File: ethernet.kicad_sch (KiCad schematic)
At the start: 1 part

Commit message: write some things down
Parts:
- U1: renamed from U?; value MCIMX6YxxVMxxxx -> MCIMX6Y2DVM09AB; Manufacturer (none) -> NXP; MfgPartNo (none) -> MCIMX6Y2DVM09AB; Vendor (none) -> Digi-Key; VendorPartNo (none) -> 568-14995-ND
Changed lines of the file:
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@@
   (symbol (lib_id "catfood:MCIMX6YxxVMxxxx") (at 55.88 53.34 0) (unit 8)
     (in_bom yes) (on_board yes) (fields_autoplaced)
-    (property "Reference" "U?" (id 0) (at 55.88 21.59 0))
-    (property "Value" "MCIMX6YxxVMxxxx" (id 1) (at 55.88 24.13 0))
+    (property "Reference" "U1" (id 0) (at 55.88 21.59 0))
+    (property "Value" "MCIMX6Y2DVM09AB" (id 1) (at 55.88 24.13 0))
     (property "Footprint" "" (id 2) (at 45.72 34.29 0)
       (effects (font (size 1.27 1.27)) hide)
@@
       (effects (font (size 1.27 1.27)) hide)
     )
+    (property "Manufacturer" "NXP" (id 4) (at 55.88 31.75 0)
+      (effects (font (size 1.27 1.27)) hide)
+    )
+    (property "MfgPartNo" "MCIMX6Y2DVM09AB" (id 5) (at 55.88 34.29 0)
+      (effects (font (size 1.27 1.27)) hide)
+    )
+    (property "Vendor" "Digi-Key" (id 6) (at 55.88 36.83 0)
+      (effects (font (size 1.27 1.27)) hide)
+    )
+    (property "VendorPartNo" "568-14995-ND" (id 7) (at 55.88 39.37 0)
+      (effects (font (size 1.27 1.27)) hide)
+    )

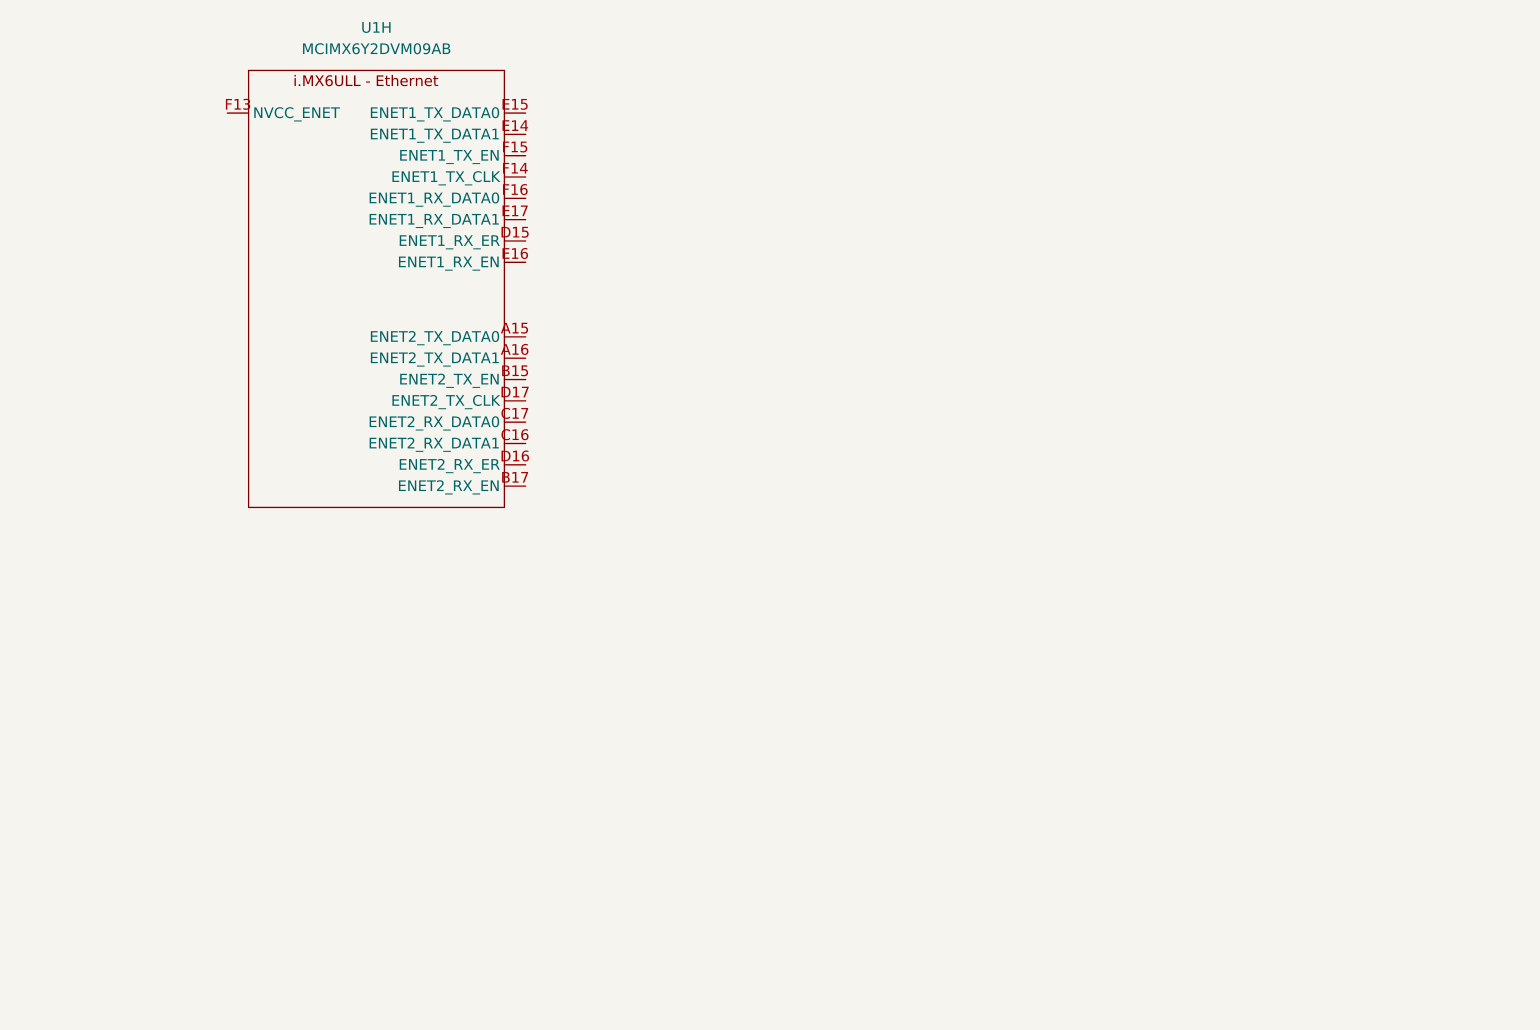
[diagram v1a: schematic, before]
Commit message: Add LAN8700 symbol
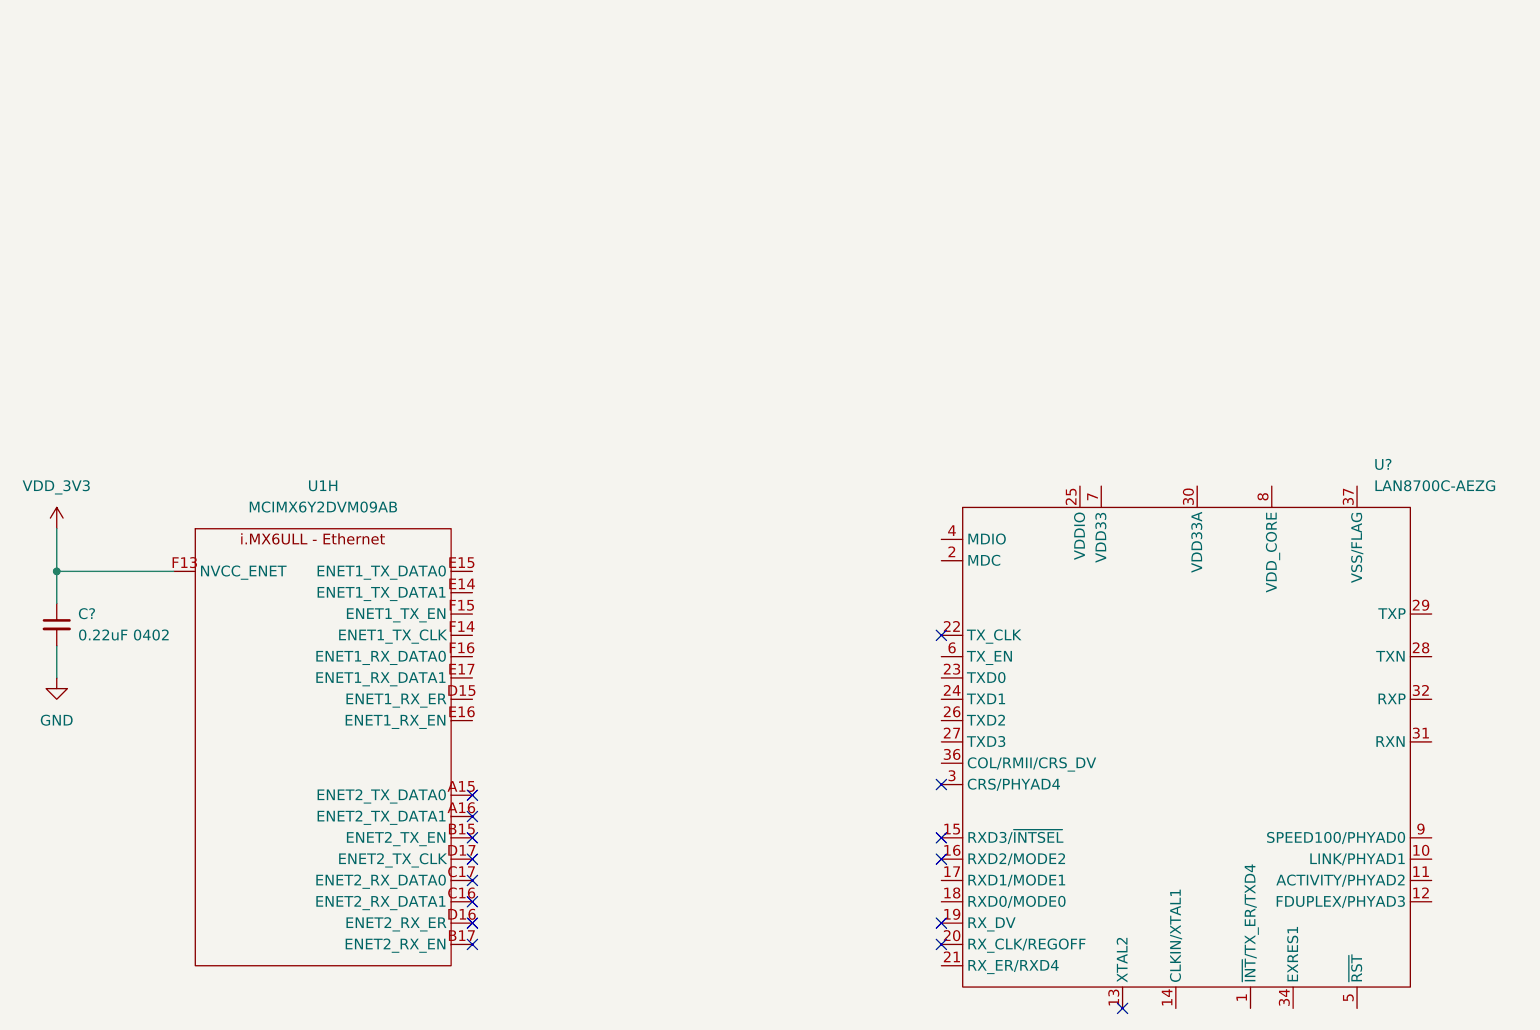
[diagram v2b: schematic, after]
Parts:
- added C?: 0.22uF 0402, symbol Device:C_Small
- added U?: LAN8700C-AEZG, symbol catfood:LAN8700C-AEZG
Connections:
- net VDD_3V3: now reaches U1.F13 (NVCC_ENET)
- net VDD_3V3: now also C?.1
- new net: U?.30 (VDD33A), U?.33 (VDD33A), U?.35 (VDD33A)
- new net GND: C?.2
- no-connect marks 0 -> 15
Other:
- moved on the sheet: U1H
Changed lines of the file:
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@@
     (company "Ian Kilgore")
   )
-  (symbol (lib_id "catfood:MCIMX6YxxVMxxxx") (at 55.88 53.34 0) (unit 8)
+  (junction (at 17.78 86.36) (diameter 0) (color 0 0 0 0)
+  )
+  (no_connect (at 67.31 130.81))
+  (no_connect (at 67.31 123.19))
+  (no_connect (at 144.78 138.43))
+  (no_connect (at 123.19 111.76))
+  (no_connect (at 67.31 113.03))
+  (no_connect (at 123.19 120.65))
+  (no_connect (at 123.19 93.98))
+  (no_connect (at 67.31 120.65))
+  (no_connect (at 123.19 118.11))
+  (no_connect (at 67.31 125.73))
+  (no_connect (at 67.31 118.11))
+  (no_connect (at 67.31 115.57))
+  (no_connect (at 123.19 130.81))
+  (no_connect (at 123.19 128.27))
+  (no_connect (at 67.31 128.27))
+  (wire (pts (xy 17.78 81.28) (xy 17.78 86.36))
+    (stroke (width 0) (type default) (color 0 0 0 0))
+  )
+  (wire (pts (xy 17.78 86.36) (xy 31.75 86.36))
+    (stroke (width 0) (type default) (color 0 0 0 0))
+  )
+  (wire (pts (xy 17.78 95.25) (xy 17.78 99.06))
+    (stroke (width 0) (type default) (color 0 0 0 0))
+  )
+  (wire (pts (xy 17.78 86.36) (xy 17.78 90.17))
+    (stroke (width 0) (type default) (color 0 0 0 0))
+  )
+  (symbol (lib_id "Device:C_Small") (at 17.78 92.71 0) (unit 1)
     (in_bom yes) (on_board yes) (fields_autoplaced)
-    (property "Reference" "U1" (id 0) (at 55.88 21.59 0))
-    (property "Value" "MCIMX6Y2DVM09AB" (id 1) (at 55.88 24.13 0))
-    (property "Footprint" "" (id 2) (at 45.72 34.29 0)
-      (effects (font (size 1.27 1.27)) hide)
-    )
-    (property "Datasheet" "" (id 3) (at 45.72 34.29 0)
-      (effects (font (size 1.27 1.27)) hide)
-    )
-    (property "Manufacturer" "NXP" (id 4) (at 55.88 31.75 0)
-      (effects (font (size 1.27 1.27)) hide)
-    )
-    (property "MfgPartNo" "MCIMX6Y2DVM09AB" (id 5) (at 55.88 34.29 0)
-      (effects (font (size 1.27 1.27)) hide)
-    )
-    (property "Vendor" "Digi-Key" (id 6) (at 55.88 36.83 0)
-      (effects (font (size 1.27 1.27)) hide)
-    )
-    (property "VendorPartNo" "568-14995-ND" (id 7) (at 55.88 39.37 0)
+    (property "Reference" "C?" (id 0) (at 20.32 91.4462 0)
+      (effects (font (size 1.27 1.27)) (justify left))
+    )
+    (property "Value" "0.22uF 0402" (id 1) (at 20.32 93.9862 0)
+      (effects (font (size 1.27 1.27)) (justify left))
+    )
+    (property "Footprint" "" (id 2) (at 17.78 92.71 0)
+      (effects (font (size 1.27 1.27)) hide)
+    )
+    (property "Datasheet" "~" (id 3) (at 17.78 92.71 0)
+      (effects (font (size 1.27 1.27)) hide)
+    )
+    (pin "1")
+    (pin "2")
+  )
+  (symbol (lib_id "catfood:MCIMX6YxxVMxxxx") (at 49.53 107.95 0) (unit 8)
+    (in_bom yes) (on_board yes) (fields_autoplaced)
+    (property "Reference" "U1" (id 0) (at 49.53 76.2 0))
+    (property "Value" "MCIMX6Y2DVM09AB" (id 1) (at 49.53 78.74 0))
+    (property "Footprint" "" (id 2) (at 39.37 88.9 0)
+      (effects (font (size 1.27 1.27)) hide)
+    )
+    (property "Datasheet" "" (id 3) (at 39.37 88.9 0)
+      (effects (font (size 1.27 1.27)) hide)
+    )
+    (property "Manufacturer" "NXP" (id 4) (at 49.53 86.36 0)
+      (effects (font (size 1.27 1.27)) hide)
+    )
+    (property "MfgPartNo" "MCIMX6Y2DVM09AB" (id 5) (at 49.53 88.9 0)
+      (effects (font (size 1.27 1.27)) hide)
+    )
+    (property "Vendor" "Digi-Key" (id 6) (at 49.53 91.44 0)
+      (effects (font (size 1.27 1.27)) hide)
+    )
+    (property "VendorPartNo" "568-14995-ND" (id 7) (at 49.53 93.98 0)
       (effects (font (size 1.27 1.27)) hide)
     )
@@
     (pin "N17")
   )
+  (symbol (lib_id "power:GND") (at 17.78 99.06 0) (unit 1)
+    (in_bom yes) (on_board yes) (fields_autoplaced)
+    (property "Reference" "#PWR?" (id 0) (at 17.78 105.41 0)
+      (effects (font (size 1.27 1.27)) hide)
+    )
+    (property "Value" "GND" (id 1) (at 17.78 104.14 0))
+    (property "Footprint" "" (id 2) (at 17.78 99.06 0)
+      (effects (font (size 1.27 1.27)) hide)
+    )
+    (property "Datasheet" "" (id 3) (at 17.78 99.06 0)
+      (effects (font (size 1.27 1.27)) hide)
+    )
+    (pin "1")
+  )
+  (symbol (lib_id "catfood:LAN8700C-AEZG") (at 125.73 82.55 0) (unit 1)
+    (in_bom yes) (on_board yes) (fields_autoplaced)
+    (property "Reference" "U?" (id 0) (at 174.7394 73.66 0)
+      (effects (font (size 1.27 1.27)) (justify left))
+    )
+    (property "Value" "LAN8700C-AEZG" (id 1) (at 174.7394 76.2 0)
+      (effects (font (size 1.27 1.27)) (justify left))
+    )
+    (property "Footprint" "" (id 2) (at 123.19 82.55 0)
+      (effects (font (size 1.27 1.27)) hide)
+    )
+    (property "Datasheet" "" (id 3) (at 123.19 82.55 0)
+      (effects (font (size 1.27 1.27)) hide)
+    )
+    (pin "1")
+    (pin "10")
+    (pin "11")
+    (pin "12")
+    (pin "13")
+    (pin "14")
+    (pin "15")
+    (pin "16")
+    (pin "17")
+    (pin "18")
+    (pin "19")
+    (pin "2")
+    (pin "20")
+    (pin "21")
+    (pin "22")
+    (pin "23")
+    (pin "24")
+    (pin "25")
+    (pin "26")
+    (pin "27")
+    (pin "28")
+    (pin "29")
+    (pin "3")
+    (pin "30")
+    (pin "31")
+    (pin "32")
+    (pin "33")
+    (pin "34")
+    (pin "35")
+    (pin "36")
+    (pin "37")
+    (pin "4")
+    (pin "5")
+    (pin "6")
+    (pin "7")
+    (pin "8")
+    (pin "9")
+  )
+  (symbol (lib_id "catfood:VDD_3V3") (at 17.78 81.28 0) (unit 1)
+    (in_bom yes) (on_board yes) (fields_autoplaced)
+    (property "Reference" "#PWR?" (id 0) (at 17.78 85.09 0)
+      (effects (font (size 1.27 1.27)) hide)
+    )
+    (property "Value" "VDD_3V3" (id 1) (at 17.78 76.2 0))
+    (property "Footprint" "" (id 2) (at 17.78 81.28 0)
+      (effects (font (size 1.27 1.27)) hide)
+    )
+    (property "Datasheet" "" (id 3) (at 17.78 81.28 0)
+      (effects (font (size 1.27 1.27)) hide)
+    )
+    (pin "1")
+  )
 )
